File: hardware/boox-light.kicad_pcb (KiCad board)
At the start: 2 copper layers, 24 parts, among them J1 USB_OTG, J2 Passthrough, Q1 BSS138P, U1 MCP73831-2-OT, U2 ATtiny85-20SU

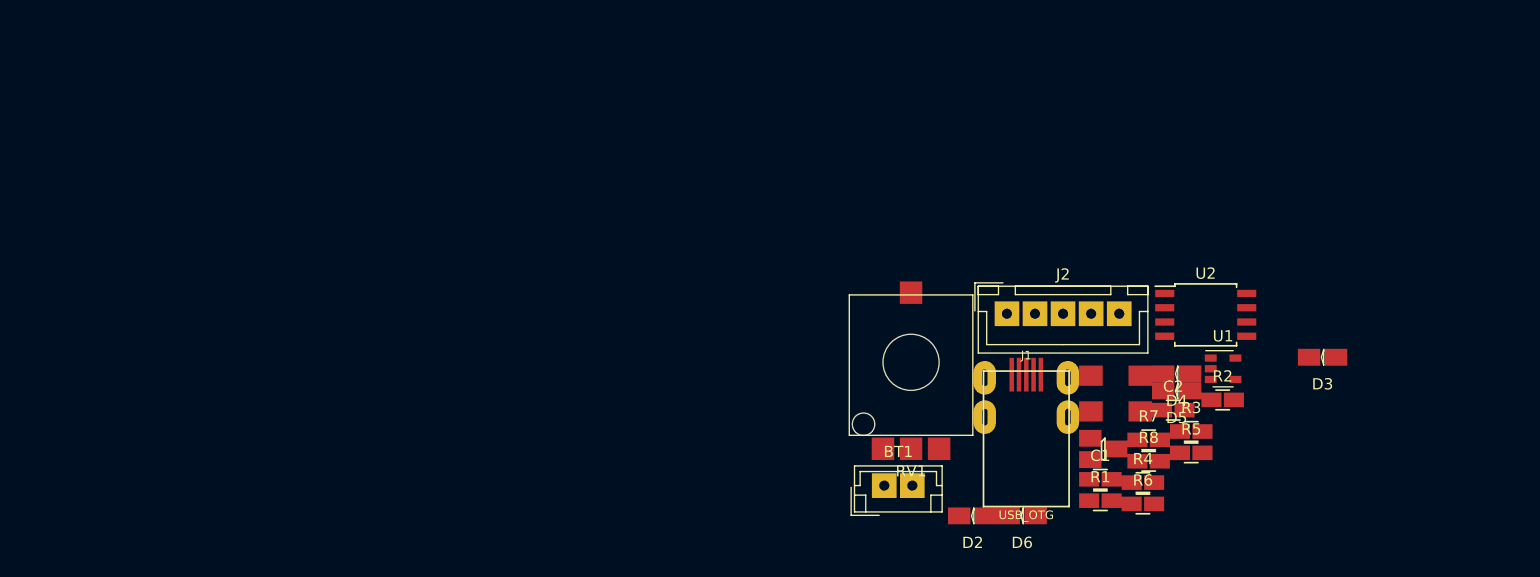
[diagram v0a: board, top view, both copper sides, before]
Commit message: Adding completed layout.
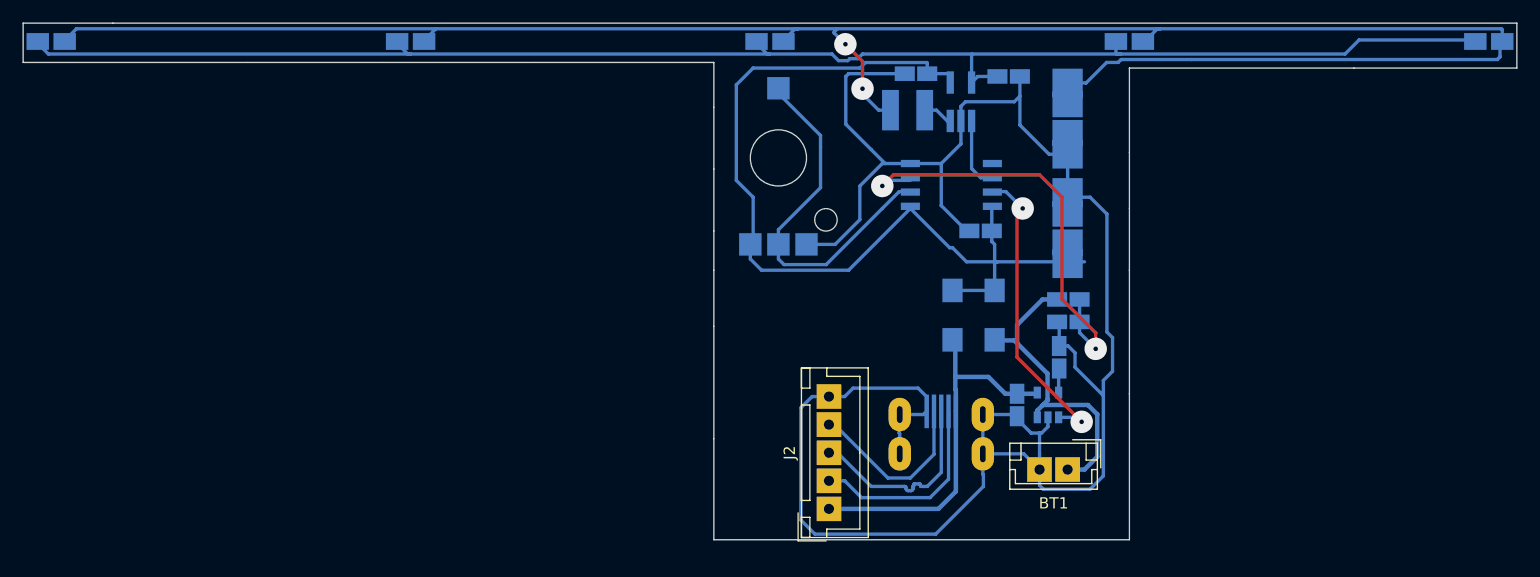
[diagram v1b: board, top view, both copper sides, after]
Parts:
- removed Q1: BSS138P, coddingtonbear:SOT-23_LargePads
- removed R3, R4, R5, R6: 20, coddingtonbear:0805_Milling
- added C3: 100uF / NTC-T107K10TRDF, coddingtonbear:CP_Tantalum_Case-D_EIA-7343-31_Milling, B.Cu at (172.5, 50.8)
- added C4: 100uF / NTC-T107K10TRDF, coddingtonbear:CP_Tantalum_Case-D_EIA-7343-31_Milling, B.Cu at (172.5, 41.0)
- added C5: 0.1u, coddingtonbear:0805_Milling, B.Cu at (159.0, 37.0)
- added L1: 47u, Inductor_SMD:L_Bourns-SRN4018, B.Cu at (158.2, 40.2)
- added U3: PAM2804, Package_TO_SOT_SMD:TSOT-23-5_HandSoldering, B.Cu at (163.0, 39.5)
- C1, C2, D1, D2, D3, D4, D5, D6, D7, J1, R1, R7, R8, RV1, U1, U2: moved to B.Cu
- R2: value 20 -> 1.0 (max); moved to B.Cu
- moved D2 92.3 mm to (82.0, 34.1)
- moved D3 85.9 mm to (114.0, 34.1)
- moved D6 59.2 mm to (210.0, 34.1)
- moved D4 46.8 mm to (146.0, 34.1)
- moved R2 34.5 mm to (167.2, 37.2)
- moved D5 31.4 mm to (178.0, 34.1)
- moved U2 25.4 mm to (162.2, 46.9)
- moved J2 23.5 mm to (151.2, 75.8), turned to 90 degrees
- moved C2 23.4 mm to (164.8, 51.0)
- moved RV1 21.7 mm to (146.8, 44.5), turned to 180 degrees
- moved D7 16.9 mm to (162.2, 58.5), turned to 270 degrees
- moved BT1 16.4 mm to (172.5, 72.2), turned to 180 degrees
- moved U1 15.9 mm to (170.8, 66.5), turned to 90 degrees
- moved R7 14.4 mm to (172.6, 57.1)
- moved R8 14.3 mm to (172.6, 59.1), turned to 180 degrees
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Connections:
- net Net-(J1-Pad4) renamed /ID
- D2 pad 1: Net-(D2-Pad1) -> /LED-
- D2 pad 2: Net-(D2-Pad2) -> /LED+
- D3 pad 1: Net-(D2-Pad1) -> /LED-
- D3 pad 2: Net-(D3-Pad2) -> /LED+
- D4 pad 1: Net-(D2-Pad1) -> /LED-
- D4 pad 2: Net-(D4-Pad2) -> /LED+
- D5 pad 1: Net-(D2-Pad1) -> /LED-
- D5 pad 2: Net-(D5-Pad2) -> /LED+
- D6 pad 1: Net-(D2-Pad1) -> /LED-
- D6 pad 2: Net-(D6-Pad2) -> /LED+
- J1 pad 2: Net-(J1-Pad2) -> /D-
- J1 pad 3: Net-(J1-Pad3) -> /D+
- J1 pad 6: Net-(J1-Pad6) -> GND
- J2 pad 2: Net-(J1-Pad3) -> /D-
- J2 pad 3: Net-(J1-Pad2) -> /D+
- R2 pad 1: Net-(D2-Pad2) -> /LED-
- R2 pad 2: VCC -> GND
- U2 pad 2: Net-(U2-Pad2) -> BRIGHTNESS
- U2 pad 3: Net-(U2-Pad3) -> BATT_VOLTAGE
- U2 pad 5: Net-(U2-Pad5) -> (no net)
- U2 pad 6: Net-(U2-Pad6) -> LED_PWM
- U2 pad 7: Net-(U2-Pad7) -> CHG_STATUS
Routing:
- net /LED+: track 0.00 -> 189.2 mm, vias 0 -> 2
- net GND: track 0.00 -> 185.4 mm
- net /LED-: track 0.00 -> 139.3 mm
- net VCC: track 0.00 -> 86.2 mm
- net BATT_VOLTAGE: track 0.00 -> 39.7 mm, vias 0 -> 2
- net +5V: track 0.00 -> 33.4 mm
- net BRIGHTNESS: track 0.00 -> 32.9 mm
- net +BATT: track 0.00 -> 28.7 mm
- net CHG_STATUS: track 0.00 -> 27.2 mm, vias 0 -> 2
- net /D+: track 0.00 -> 18.1 mm
- net /D-: track 0.00 -> 18.0 mm
- net /ID: track 0.00 -> 16.0 mm
- net LED_PWM: track 0.00 -> 6.43 mm
- net Net-(L1-Pad1): track 0.00 -> 2.64 mm
- net Net-(R1-Pad2): track 0.00 -> 2.17 mm
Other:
- board outline added: 133 x 46 mm
- net class Default: clearance 0.2 -> 0.19; trace_width 0.25 -> 0.3; via_dia 0.8 -> 2
- net class Power added: clearance 0.19, trace_width 0.4, via_dia 2, via_drill 0.4
- rule trace_clearance: 0.2 -> 0.19
